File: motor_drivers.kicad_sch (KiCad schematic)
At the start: 24 parts, among them Q2 2N7002, U7 AMS1117-3.3, U8 TB6612FNG, U9 TB6612FNG

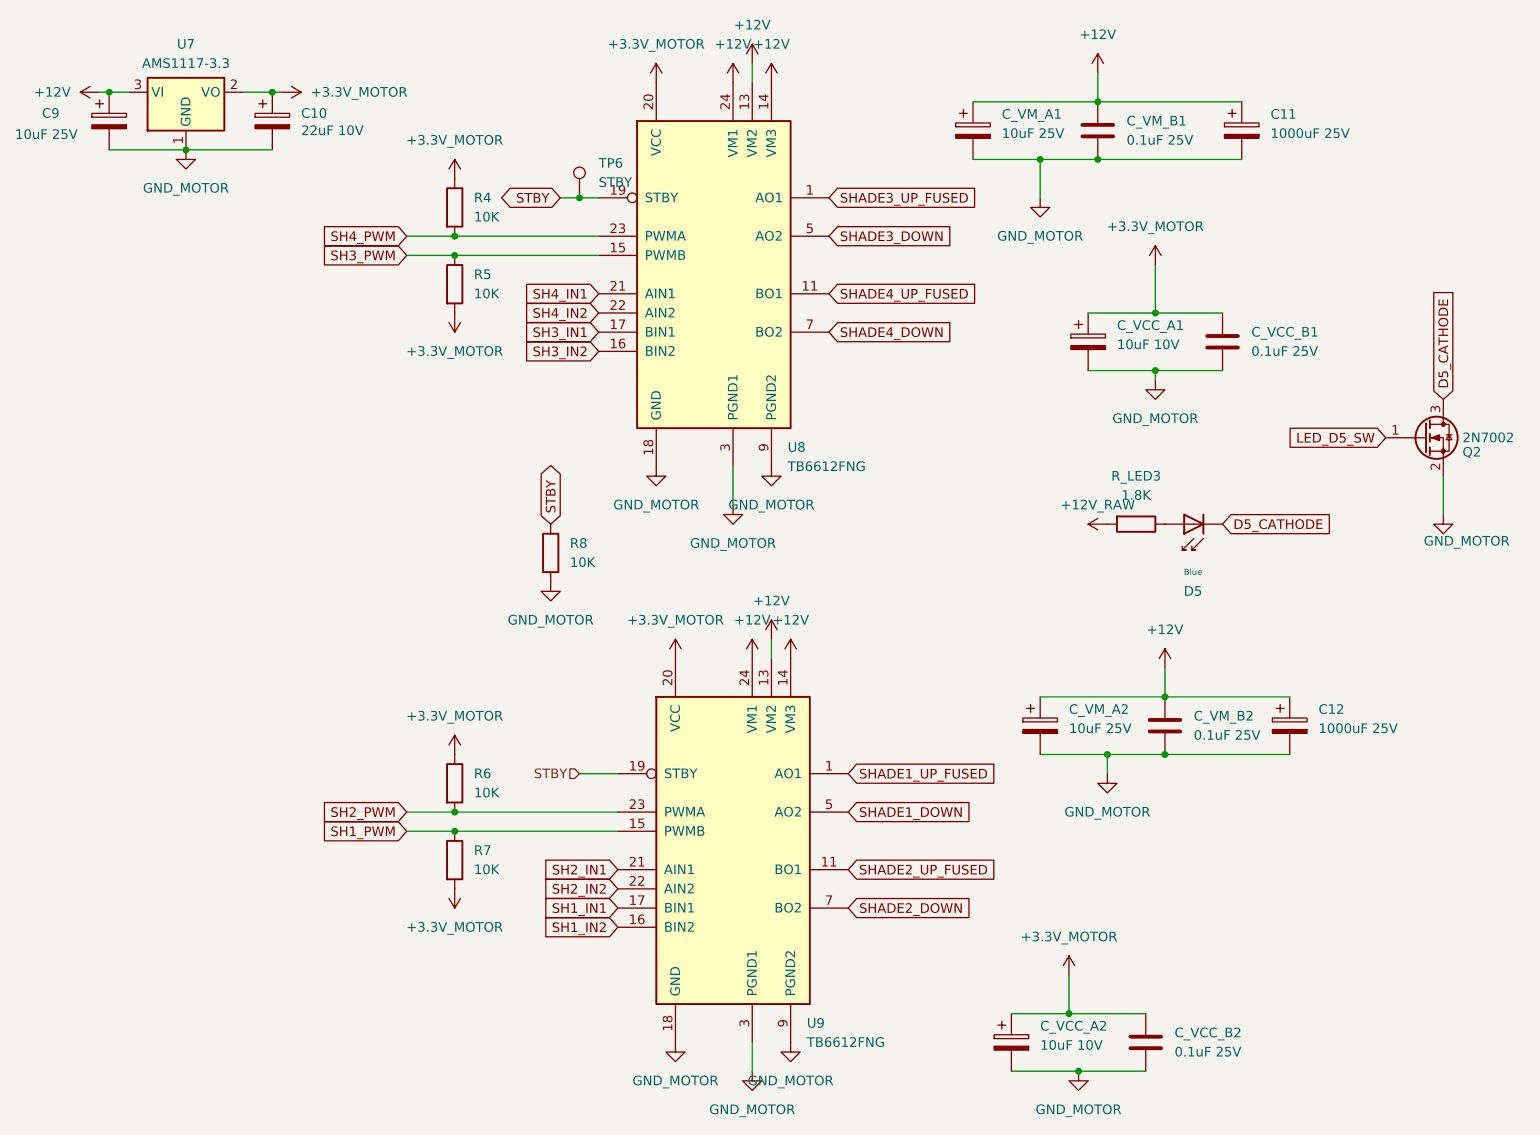
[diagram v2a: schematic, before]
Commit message: Update annotations, fixed font sizes.
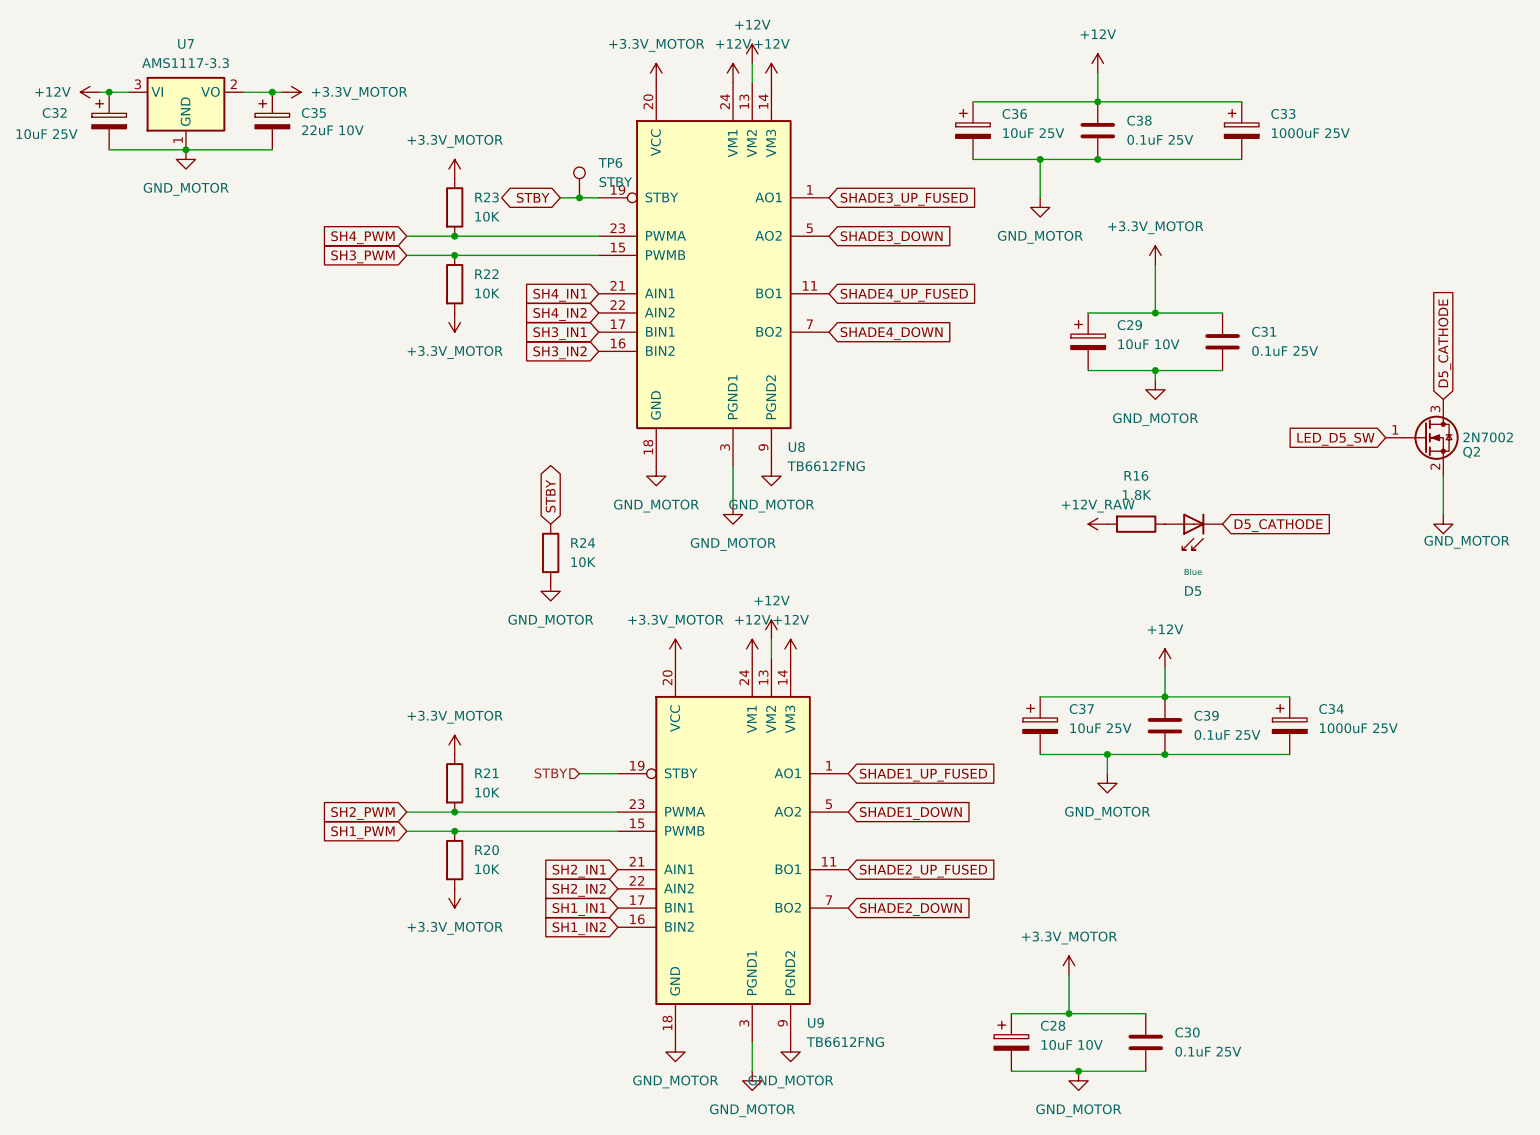
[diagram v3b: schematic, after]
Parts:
- renumbered C_VCC_A2 to C28, C_VCC_A1 to C29, C_VCC_B2 to C30, C_VCC_B1 to C31, C9 to C32, C11 to C33, C12 to C34, C10 to C35, C_VM_A1 to C36, C_VM_A2 to C37, C_VM_B1 to C38, C_VM_B2 to C39, R_LED3 to R16, R7 to R20, R6 to R21, R5 to R22, R4 to R23, R8 to R24
